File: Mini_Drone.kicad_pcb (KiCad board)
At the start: 4 copper layers, 94.2 x 113.7 mm, 34 parts, among them J1 Conn_01x02, J3 Conn_01x02, J4 Conn_01x06, J7 Conn_01x11, J8 Conn_01x11, SW2 Tactile Switch 3x4x2, SW3 Tactile Switch 3x4x2, U1 ESP32-S3-WROOM-1, U2 MPU_6050_Module, U3 SPX3819M5-L-3-3

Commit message: main board completed need to tidy up the routing , motor driver yet to be completed
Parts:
- TP18: value D0 -> M1
- TP19: value D0 -> M2
- TP20: value D0 -> M3
- TP21: value D0 -> M4
- TP22, TP23, TP24, TP25: value D0 -> BAT+
- TP26, TP27, TP28, TP29: value D0 -> GND
- moved TP26 7.69 mm to (193.7, 83.2)
- moved TP18 7.67 mm to (193.9, 75.8)
- moved R8 0.51 mm to (228.2, 93.6)
- moved TP22 0.10 mm to (193.6, 79.4)
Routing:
- net /M1: track 30.9 -> 38.8 mm
- net GND: track 64.2 -> 65.2 mm
- net /IO48: track 15.4 -> 14.7 mm
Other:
- board text added: "AD0"
- board text added: "BAT+"
- board text added: "EN"
- board text added: "GND"
- board text added: "INT"
- board text added: "IO0"
- board text added: "IO10"
- board text added: "IO11"
- board text added: "IO12"
- board text added: "IO13"
- board text added: "IO14"
- board text added: "IO15"
- board text added: "IO21"
- board text added: "IO35"
- board text added: "IO36"
- board text added: "IO37"
- board text added: "IO38"
- board text added: "IO39"
- board text added: "IO41"
- board text added: "IO42"
- board text added: "IO47"
- board text added: "IO48"
- board text added: "IO49"
- board text added: "IO6"
- board text added: "IO7"
- board text added: "IO8"
- board text added: "IO9"
- board text added: "M1"
- board text added: "M2"
- board text added: "M3"
- board text added: "M4"
- board text added: "RX0"
- board text added: "SCL"
- board text added: "SDA"
- board text added: "TX0"
- board text added: "USBD+"
- board text added: "USBD-"
- board text added: "VCC"
- board text added: "XCL"
- board text added: "XDA"

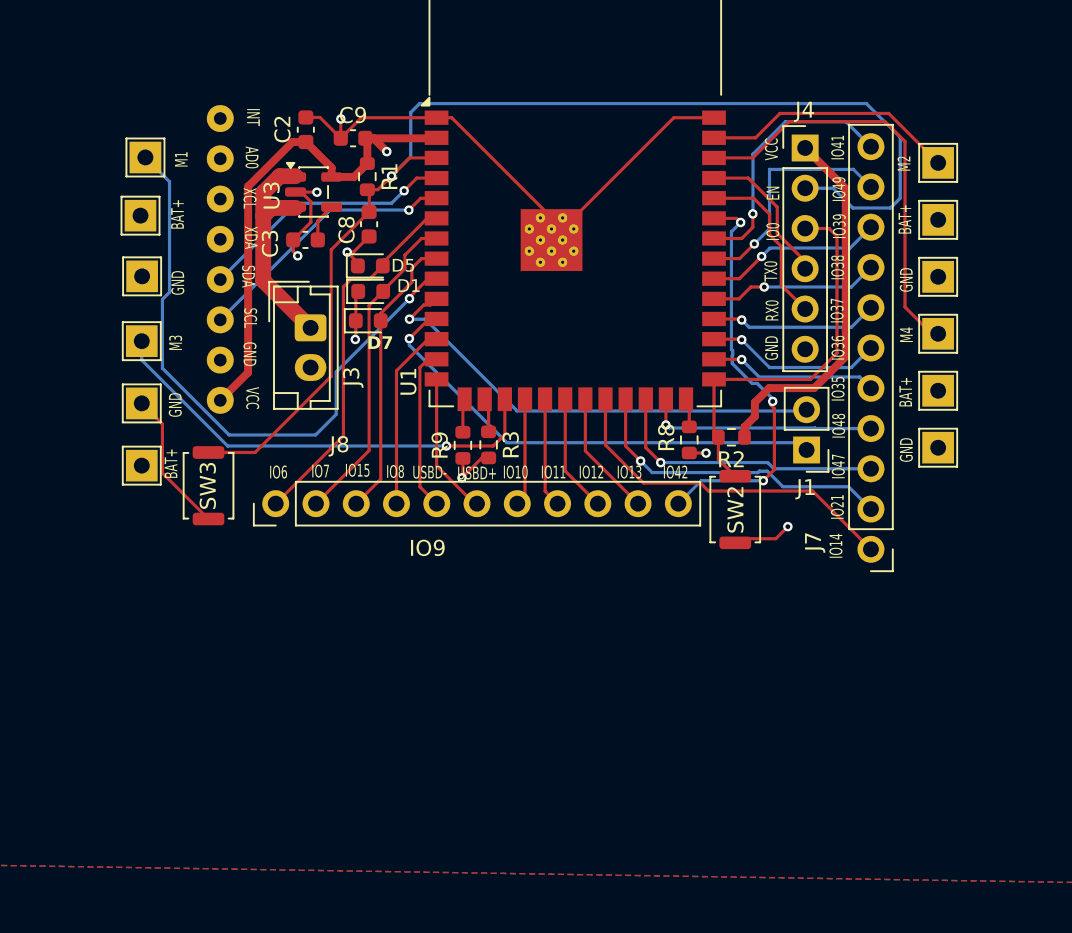
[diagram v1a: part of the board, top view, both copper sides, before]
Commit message: motor driver circuit need to do the outline
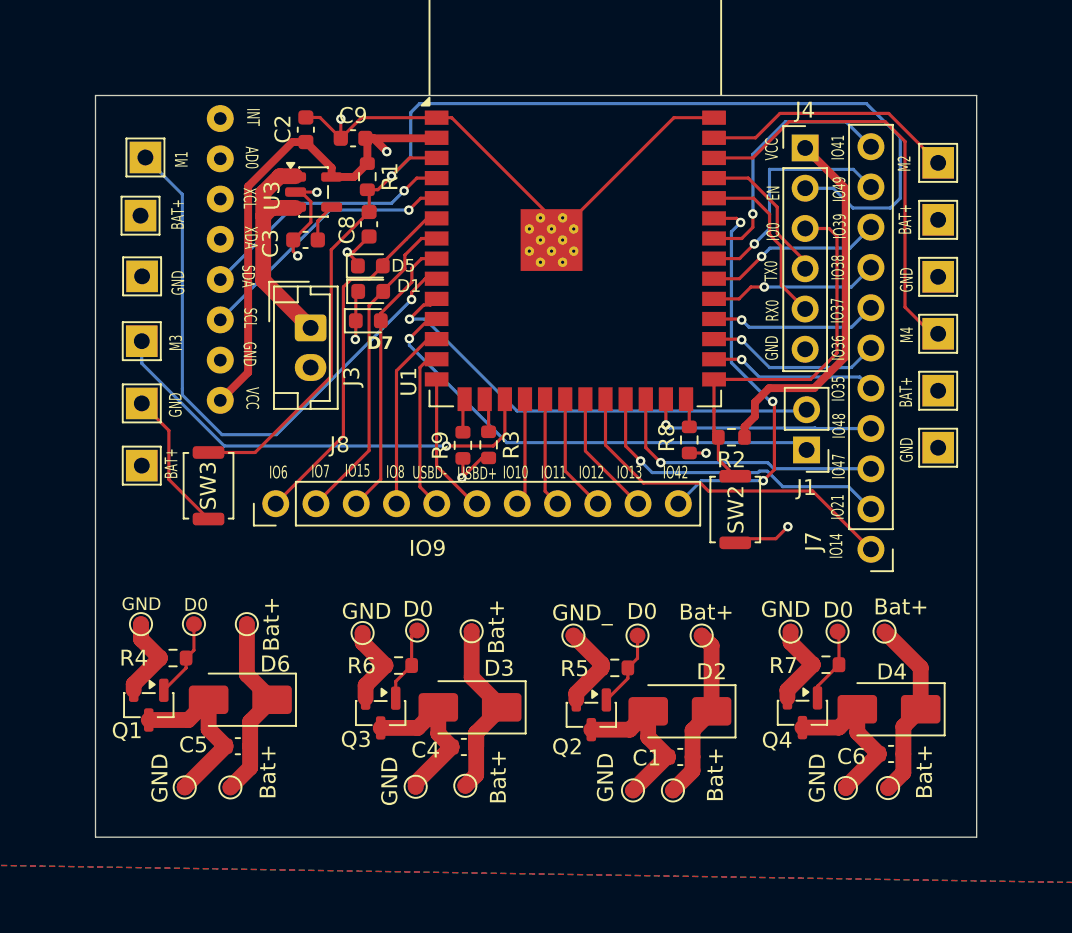
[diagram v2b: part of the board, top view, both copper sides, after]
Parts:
- added C1: 1uf, Capacitor_SMD:C_0603_1608Metric, F.Cu at (227.6, 113.6)
- added C4: 1uf, Capacitor_SMD:C_0603_1608Metric, F.Cu at (214.0, 112.9)
- added C5: 1uf, Capacitor_SMD:C_0603_1608Metric, F.Cu at (199.7, 112.9)
- added C6: 1uf, Capacitor_SMD:C_0603_1608Metric, F.Cu at (240.9, 113.4)
- added D2: SS34, Diode_SMD:D_SMA, F.Cu at (227.6, 110.7)
- added D3: SS34, Diode_SMD:D_SMA, F.Cu at (214.4, 110.4)
- added D4: SS34, Diode_SMD:D_SMA, F.Cu at (240.8, 110.6)
- added D6: SS34, Diode_SMD:D_SMA, F.Cu at (199.9, 110.0)
- added Q1: AO3400A, Package_TO_SOT_SMD:SOT-23, F.Cu at (194.1, 110.3)
- added Q2: AO3400A, Package_TO_SOT_SMD:SOT-23, F.Cu at (222.0, 110.9)
- added Q3: AO3400A, Package_TO_SOT_SMD:SOT-23, F.Cu at (208.7, 110.8)
- added Q4: AO3400A, Package_TO_SOT_SMD:SOT-23, F.Cu at (235.3, 110.8)
- added R4: 10k, Resistor_SMD:R_0603_1608Metric, F.Cu at (195.6, 107.3)
- added R5: 10k, Resistor_SMD:R_0603_1608Metric, F.Cu at (223.5, 108.0)
- added R6: 10k, Resistor_SMD:R_0603_1608Metric, F.Cu at (209.8, 107.8)
- added R7: 10k, Resistor_SMD:R_0603_1608Metric, F.Cu at (236.8, 107.8)
- added TP1: Bat+, TestPoint:TestPoint_Pad_D1.0mm, F.Cu at (199.2, 115.5)
- added TP10: Bat+, TestPoint:TestPoint_Pad_D1.0mm, F.Cu at (214.1, 115.4)
- added TP11: GND, TestPoint:TestPoint_Pad_D1.0mm, F.Cu at (193.6, 105.2)
- added TP12: GND, TestPoint:TestPoint_Pad_D1.0mm, F.Cu at (207.6, 105.8)
- added TP13: GND, TestPoint:TestPoint_Pad_D1.0mm, F.Cu at (210.9, 115.5)
- added TP14: Bat+, TestPoint:TestPoint_Pad_D1.0mm, F.Cu at (214.5, 105.6)
- added TP15: D0, TestPoint:TestPoint_Pad_D1.0mm, F.Cu at (237.5, 105.7)
- added TP16: Bat+, TestPoint:TestPoint_Pad_D1.0mm, F.Cu at (240.5, 105.7)
- added TP17: GND, TestPoint:TestPoint_Pad_D1.0mm, F.Cu at (234.6, 105.7)
- added TP2: D0, TestPoint:TestPoint_Pad_D1.0mm, F.Cu at (224.9, 105.9)
- added TP3: Bat+, TestPoint:TestPoint_Pad_D1.0mm, F.Cu at (227.2, 115.7)
- added TP30: Bat+, TestPoint:TestPoint_Pad_D1.0mm, F.Cu at (200.3, 105.2)
- added TP31: GND, TestPoint:TestPoint_Pad_D1.0mm, F.Cu at (238.1, 115.5)
- added TP32: Bat+, TestPoint:TestPoint_Pad_D1.0mm, F.Cu at (240.7, 115.5)
- added TP4: GND_, TestPoint:TestPoint_Pad_D1.0mm, F.Cu at (220.9, 105.9)
- added TP5: GND, TestPoint:TestPoint_Pad_D1.0mm, F.Cu at (196.4, 115.5)
- added TP6: GND, TestPoint:TestPoint_Pad_D1.0mm, F.Cu at (224.6, 115.7)
- added TP7: Bat+, TestPoint:TestPoint_Pad_D1.0mm, F.Cu at (229.0, 105.9)
- added TP8: D0, TestPoint:TestPoint_Pad_D1.0mm, F.Cu at (211.0, 105.6)
- added TP9: D0, TestPoint:TestPoint_Pad_D1.0mm, F.Cu at (196.9, 105.2)
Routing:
- net Net-(D3-K): track 0.00 -> 12.4 mm
- net Net-(D6-K): track 0.00 -> 12.0 mm
- net Net-(D4-K): track 0.00 -> 11.7 mm
- net Net-(D6-A): track 0.00 -> 11.3 mm
- net Net-(D2-K): track 0.00 -> 11.0 mm
- net Net-(D2-A): track 0.00 -> 10.5 mm
- net Net-(D3-A): track 0.00 -> 10.5 mm
- net Net-(D4-A): track 0.00 -> 10.3 mm
- net Net-(Q2-S): track 0.00 -> 5.46 mm
- net Net-(Q4-S): track 0.00 -> 5.43 mm
- net Net-(Q1-S): track 0.00 -> 5.35 mm
- net Net-(Q3-S): track 0.00 -> 5.23 mm
- net /M1_: track 0.00 -> 4.96 mm
- net /M2_: track 0.00 -> 4.87 mm
- net /M3_: track 0.00 -> 4.83 mm
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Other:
- outline, holes or cut-outs redrawn

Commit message: first prototype need to make the driver circuits symmetric and check everything assembly files yet to be made
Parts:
- added REF**: MouseBite-Part_2.0x2.0mm_inset_D0.5mm_P0.85mm_5h, Panelization:MouseBite-Part_2.0x2.0mm_inset_D0.5mm_P0.85mm_5h, F.Cu at (225.0, 104.0)
- added REF**: MouseBite-Part_2.0x2.0mm_inset_D0.5mm_P0.85mm_5h, Panelization:MouseBite-Part_2.0x2.0mm_inset_D0.5mm_P0.85mm_5h, F.Cu at (211.0, 104.0)
- added REF**: MouseBite-Part_2.0x2.0mm_inset_D0.5mm_P0.85mm_5h, Panelization:MouseBite-Part_2.0x2.0mm_inset_D0.5mm_P0.85mm_5h, F.Cu at (238.0, 104.0)
- added REF**: MouseBite-Part_2.0x2.0mm_inset_D0.5mm_P0.85mm_5h, Panelization:MouseBite-Part_2.0x2.0mm_inset_D0.5mm_P0.85mm_5h, F.Cu at (196.0, 104.0)
- moved Q1 2.03 mm to (193.2, 112.1)
- moved TP1 2.03 mm to (198.4, 117.3)
- moved TP11 2.03 mm to (192.7, 107.0)
- moved TP30 2.03 mm to (199.4, 107.0)
- moved TP5 2.03 mm to (195.5, 117.3)
- moved TP9 2.03 mm to (196.1, 107.0)
- moved C5 2.03 mm to (198.8, 114.7)
- moved R4 2.03 mm to (194.8, 109.2)
- moved C4 1.73 mm to (214.0, 114.7)
- moved Q3 1.73 mm to (208.7, 112.5)
- moved R6 1.73 mm to (209.8, 109.5)
- moved TP10 1.73 mm to (214.1, 117.1)
- moved TP12 1.73 mm to (207.6, 107.5)
- moved TP14 1.73 mm to (214.5, 107.4)
- moved TP13 1.73 mm to (210.9, 117.2)
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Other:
- board size 94.2 x 113.7 mm -> 55 x 47 mm

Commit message: Hari's update
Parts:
- removed SW2, SW3: Tactile Switch 3x4x2, Button_Switch_SMD:SW_Push_SPST_NO_Alps_SKRK
- added S1: TL1105F160Q, Mini_Drone_prj:SW_TL1105F160Q, F.Cu at (233.5, 100.5)
- added S2: TL1105F160Q, Mini_Drone_prj:SW_TL1105F160Q, F.Cu at (195.5, 100.0)
- added S3: 100SP1T1B4M2QE, Mini_Drone_prj:SW_100SP1T1B4M2QE, F.Cu at (254.8, 102.5)
- moved R6 2.49 mm to (207.7, 110.8)
- moved REF** 2.36 mm to (240.0, 105.2)
- moved REF** 2.02 mm to (197.6, 105.2)
- moved TP12 1.97 mm to (206.2, 108.9)
- moved TP13 1.97 mm to (209.5, 118.6)
- moved TP8 1.97 mm to (209.6, 108.7)
- moved C4 1.97 mm to (212.6, 116.0)
- moved D3 1.97 mm to (212.9, 112.9)
- moved Q3 1.97 mm to (207.3, 113.9)
- moved TP10 1.97 mm to (212.7, 118.5)
- moved TP14 1.97 mm to (213.1, 108.8)
- moved C6 1.75 mm to (242.1, 116.1)
- moved TP15 1.75 mm to (238.8, 108.4)
- moved TP16 1.75 mm to (241.7, 108.4)
- moved TP31 1.75 mm to (239.3, 118.2)
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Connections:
- Q2 pad 2: Net-(Q2-S) -> unconnected-(Q2-S-Pad2)
- Q3 pad 2: Net-(Q3-S) -> unconnected-(Q3-S-Pad2)
- Q4 pad 2: Net-(Q4-S) -> unconnected-(Q4-S-Pad2)
- R5 pad 2: Net-(Q2-S) -> Net-(R5-Pad2)
- R6 pad 2: Net-(Q3-S) -> Net-(R6-Pad2)
- R7 pad 2: Net-(Q4-S) -> Net-(R7-Pad2)
- TP12 pad 1: Net-(Q3-S) -> Net-(R6-Pad2)
- TP17 pad 1: Net-(Q4-S) -> Net-(R7-Pad2)
- TP4 pad 1: Net-(Q2-S) -> Net-(R5-Pad2)
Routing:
- net (no net): track 0.00 -> 13.3 mm
- net /IO0: track 24.7 -> 33.9 mm
- net /EN: track 74.9 -> 83.4 mm
- net GND: track 65.2 -> 58.9 mm, vias 8 -> 7
- net Net-(Q2-S): track 5.46 -> 0.00 mm
- net Net-(Q4-S): track 5.43 -> 0.00 mm
- net Net-(Q3-S): track 5.23 -> 0.00 mm
- net /IO14: track 22.4 -> 23.4 mm, vias 0 -> 2
- net Net-(Q1-S): track 5.35 -> 4.46 mm
- net Net-(D4-A): track 10.3 -> 11.0 mm
- net /M1_: track 4.96 -> 5.59 mm
- net /M2_: track 4.87 -> 5.46 mm
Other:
- board size 55 x 47 mm -> 55.5 x 48.3 mm
